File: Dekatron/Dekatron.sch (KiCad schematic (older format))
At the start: 26 parts, among them Q1 Q_NMOS_GDS, T1 Transformer_1P_1S, U1 LM3478, U2 OG-8_Dekatron

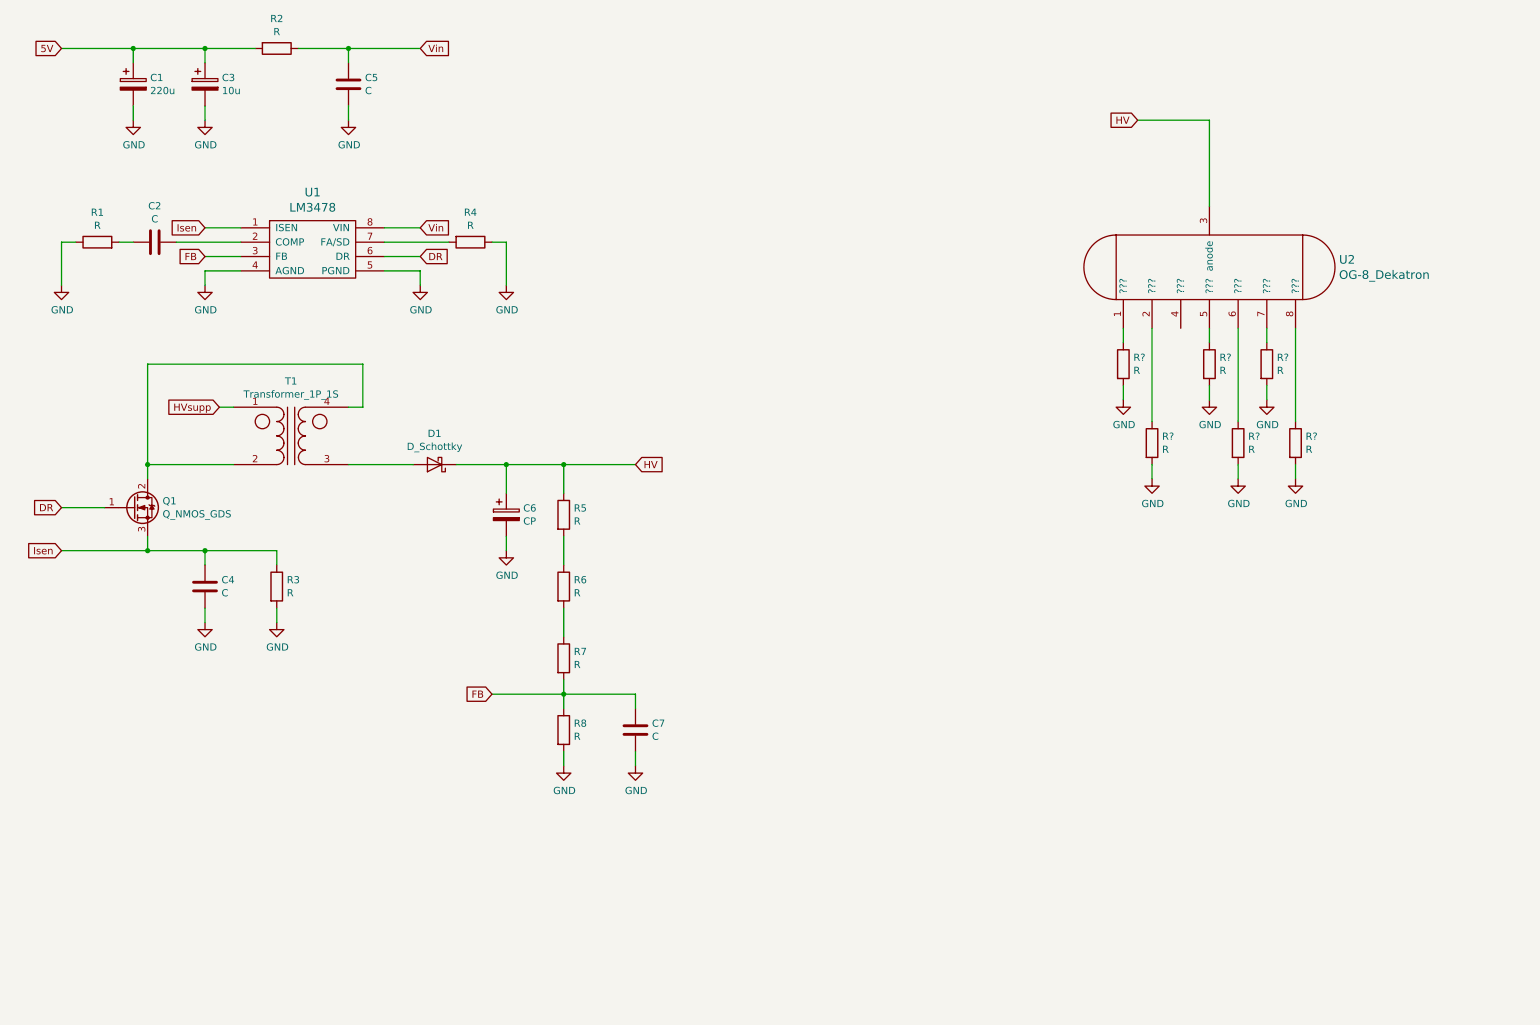
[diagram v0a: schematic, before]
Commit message: Added a breakout board to test the footprint
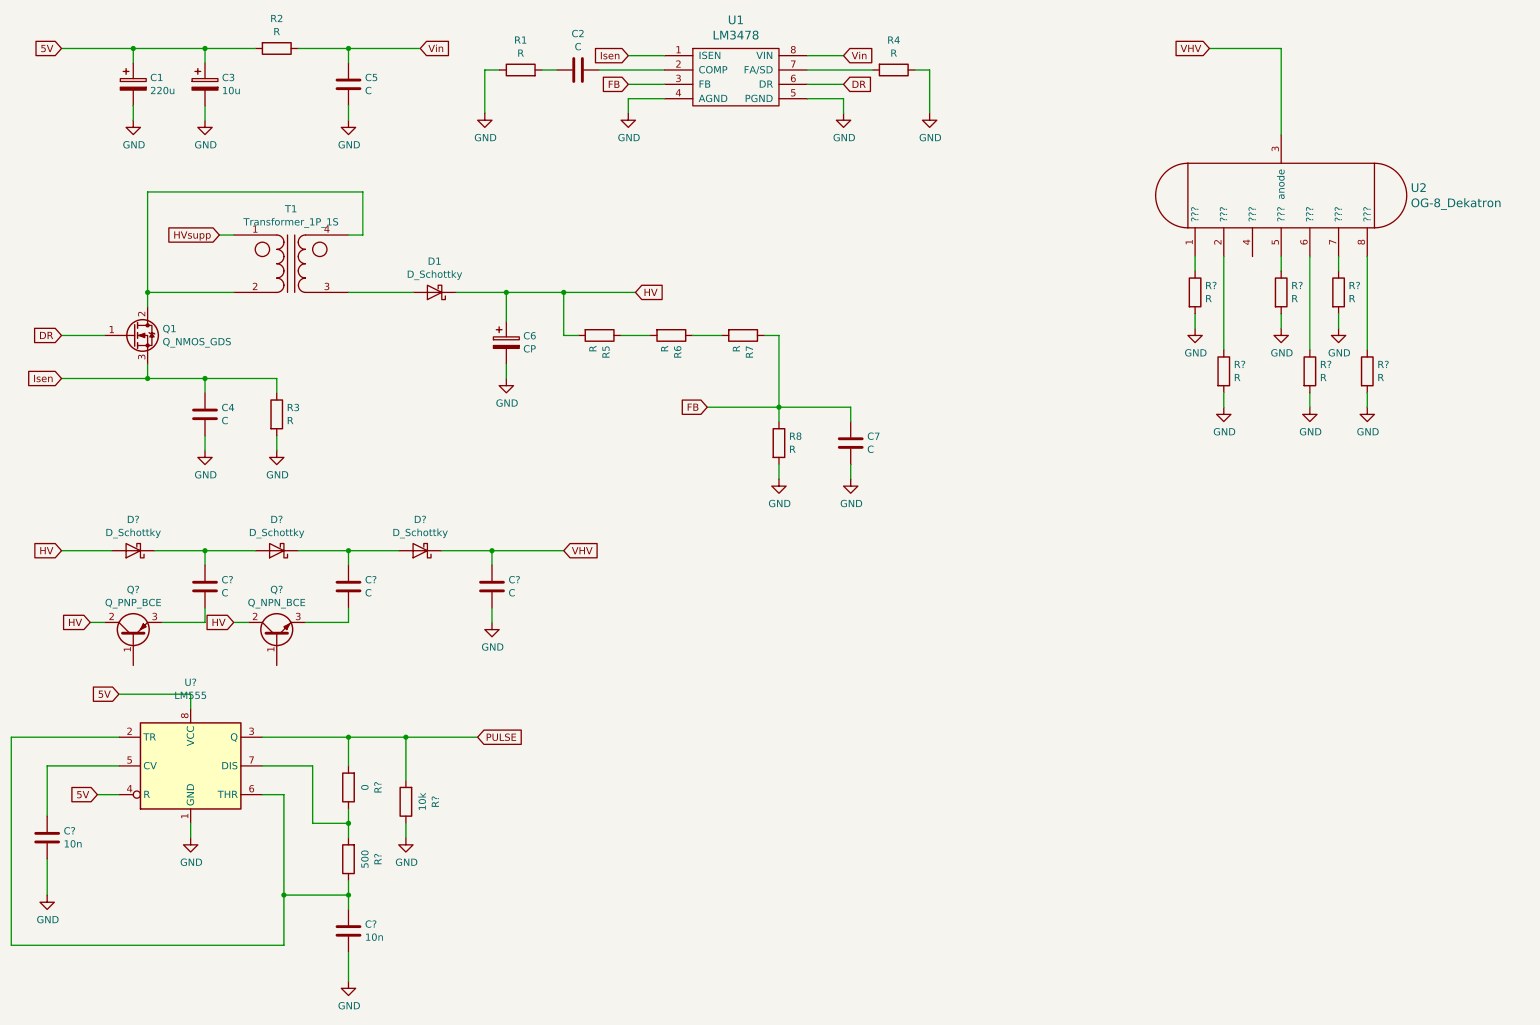
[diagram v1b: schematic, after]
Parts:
- added C? (x3): C, symbol Device:C
- added C? (x2): 10n, symbol Device:C
- added D? (x3): D_Schottky, symbol Device:D_Schottky
- added Q?: Q_PNP_BCE, symbol Device:Q_PNP_BCE
- added Q?: Q_NPN_BCE, symbol Device:Q_NPN_BCE
- added R?: 10k, symbol Device:R
- added R?: 0, symbol Device:R
- added R?: 500, symbol Device:R
- added U?: LM555, symbol Timer:LM555
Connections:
- net 5V: now also U?.4 (R), U?.8 (VCC)
- net FB: now also R7.1; no longer R7.2
- net GND: now also C?.2, C?.2, C?.2, R?.1, U?.1 (GND)
- net HV: now also R5.2, D?.2 (A), Q?.2 (C), Q?.2 (C); no longer R5.1, U2.3 (anode)
- net at R6.1: now also R7.2; no longer R5.2
- net at R6.2: now also R5.1; no longer R7.1
- new net: C?.1, D?.1 (K), D?.2 (A) (x2)
- new net: C?.2, Q?.3 (E) (x2)
- new net: C?.1, R?.1, U?.2 (TR), U?.6 (THR)
- new net: C?.1, U?.5 (CV)
- new net: R?.1, R?.2, U?.7 (DIS)
- new net PULSE: R?.2, R?.2, U?.3 (Q)
- new net VHV: C?.1, D?.1 (K), U2.3 (anode)
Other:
- moved on the sheet: C2, C4, C6, C7, D1, Q1, R1, R3, R4, R5, R6, R7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

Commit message: Developed PSU topology
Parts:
- removed C1: 220u, symbol Device:CP
- removed C2, C4, C5, C7, C? (x3): C, symbol Device:C
- removed C3: 10u, symbol Device:CP
- removed C6: CP, symbol Device:CP
- removed C? (x2): 10n, symbol Device:C
- removed D1, D? (x3): D_Schottky, symbol Device:D_Schottky
- removed Q1: Q_NMOS_GDS, symbol Device:Q_NMOS_GDS
- removed Q?: Q_PNP_BCE, symbol Device:Q_PNP_BCE
- removed Q?: Q_NPN_BCE, symbol Device:Q_NPN_BCE
- removed R1, R2, R3, R4, R5, R6, R7, R8, R?: R, symbol Device:R
- removed R?: 10k, symbol Device:R
- removed R?: 0, symbol Device:R
- removed R?: 500, symbol Device:R
- removed T1: Transformer_1P_1S, symbol Nixies:Transformer_1P_1S
- removed U1: LM3478, symbol Bamboulibs:LM3478
- removed U?: LM555, symbol Timer:LM555
- added C?: 1u, symbol Device:C
- added D?: DIODE, symbol pspice:DIODE
- added R?: 150k, symbol Device:R
- added RV?: 120k, symbol Device:R_POT
- added U?: WeMos_mini, symbol bambouLab:WeMos_mini
- R? (x4): value R -> 7k5
- U2: symbol Bamboulibs:OG-8_Dekatron -> Dekatron-rescue:OG-8_Dekatron-Bamboulibs
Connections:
- net GND: now also D?.1 (K), U?.2 (GND)
- net VHV: now also RV?.1, RV?.2; no longer U2.3 (anode)
- net at U2.4 (PK): now also C?.1, D?.2 (A)
- new net: R?.1, U2.3 (anode)
- new net: R?.2, RV?.3
- new net INC: C?.2
- new net PSU/5V: U?.1 (5V)
- no-connect marks 0 -> 2
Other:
- moved on the sheet: R?
